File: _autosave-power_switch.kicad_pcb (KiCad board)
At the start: 2 copper layers, 140 x 42.5 mm, 51 parts, among them P1 CONN_2, P10 CONN_2, P11 CONN_2, P12 CONN_2, P13 CONN_02X01, P2 CONN_2, P20 CONN_2, P3 CONN_2, P4 CONN_2, P5 CONN_2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

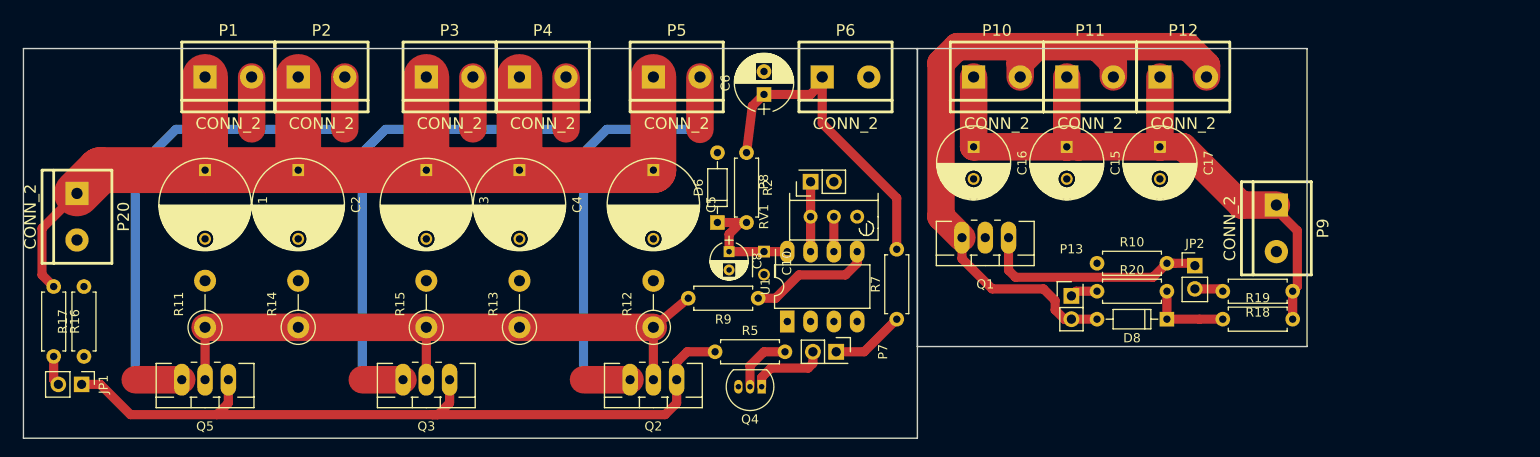
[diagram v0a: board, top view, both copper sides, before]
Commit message: powerswitch with tracks
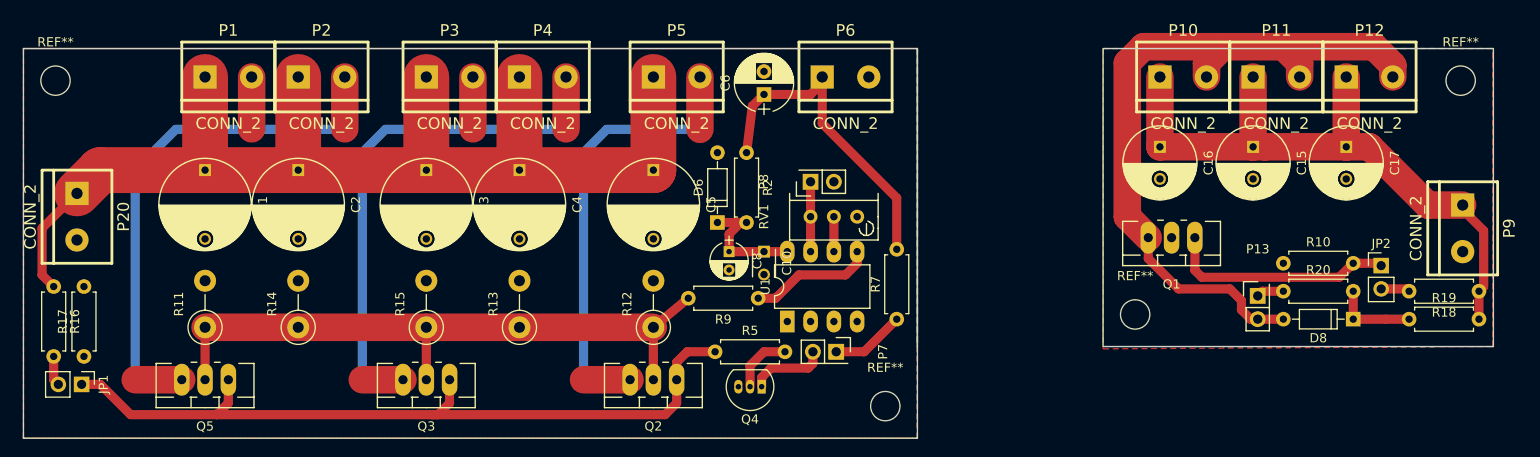
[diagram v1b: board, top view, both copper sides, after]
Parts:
- added REF**: MountingHole_3.2mm_M3, Mounting_Holes:MountingHole_3.2mm_M3, F.Cu at (141.5, 74.0)
- added REF**: MountingHole_3.2mm_M3, Mounting_Holes:MountingHole_3.2mm_M3, F.Cu at (204.2, 38.5)
- added REF**: MountingHole_3.2mm_M3, Mounting_Holes:MountingHole_3.2mm_M3, F.Cu at (168.8, 64.0)
- added REF**: MountingHole_3.2mm_M3, Mounting_Holes:MountingHole_3.2mm_M3, F.Cu at (51.0, 38.5)
- moved C15 20.3 mm to (181.6, 45.7)
- moved C17 20.3 mm to (191.8, 45.7)
- moved D8 20.3 mm to (192.5, 64.5)
- moved JP2 20.3 mm to (195.6, 58.7)
- moved P10 20.3 mm to (174.0, 38.1)
- moved C16 20.3 mm to (171.4, 45.7)
- moved P11 20.3 mm to (184.2, 38.1)
- moved P12 20.3 mm to (194.3, 38.1)
- moved P13 20.3 mm to (182.1, 62.0)
- moved P9 20.3 mm to (204.5, 54.6)
- moved Q1 20.3 mm to (172.7, 55.6)
- moved R10 20.3 mm to (184.9, 58.4)
- moved R18 20.3 mm to (206.2, 61.5)
- moved R19 20.3 mm to (198.6, 64.5)
- moved R20 20.3 mm to (184.9, 61.5)
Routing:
- added copper zone on F.Cu, net GNDA
- added copper zone on F.Cu, net GNDPWR
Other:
- board size 140 x 42.5 mm -> 160.3 x 42.5 mm
